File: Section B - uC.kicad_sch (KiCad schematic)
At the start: 8 parts, among them J1 Conn_ARM_SWD_TagConnect_TC203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, U1 ATtiny204-SS

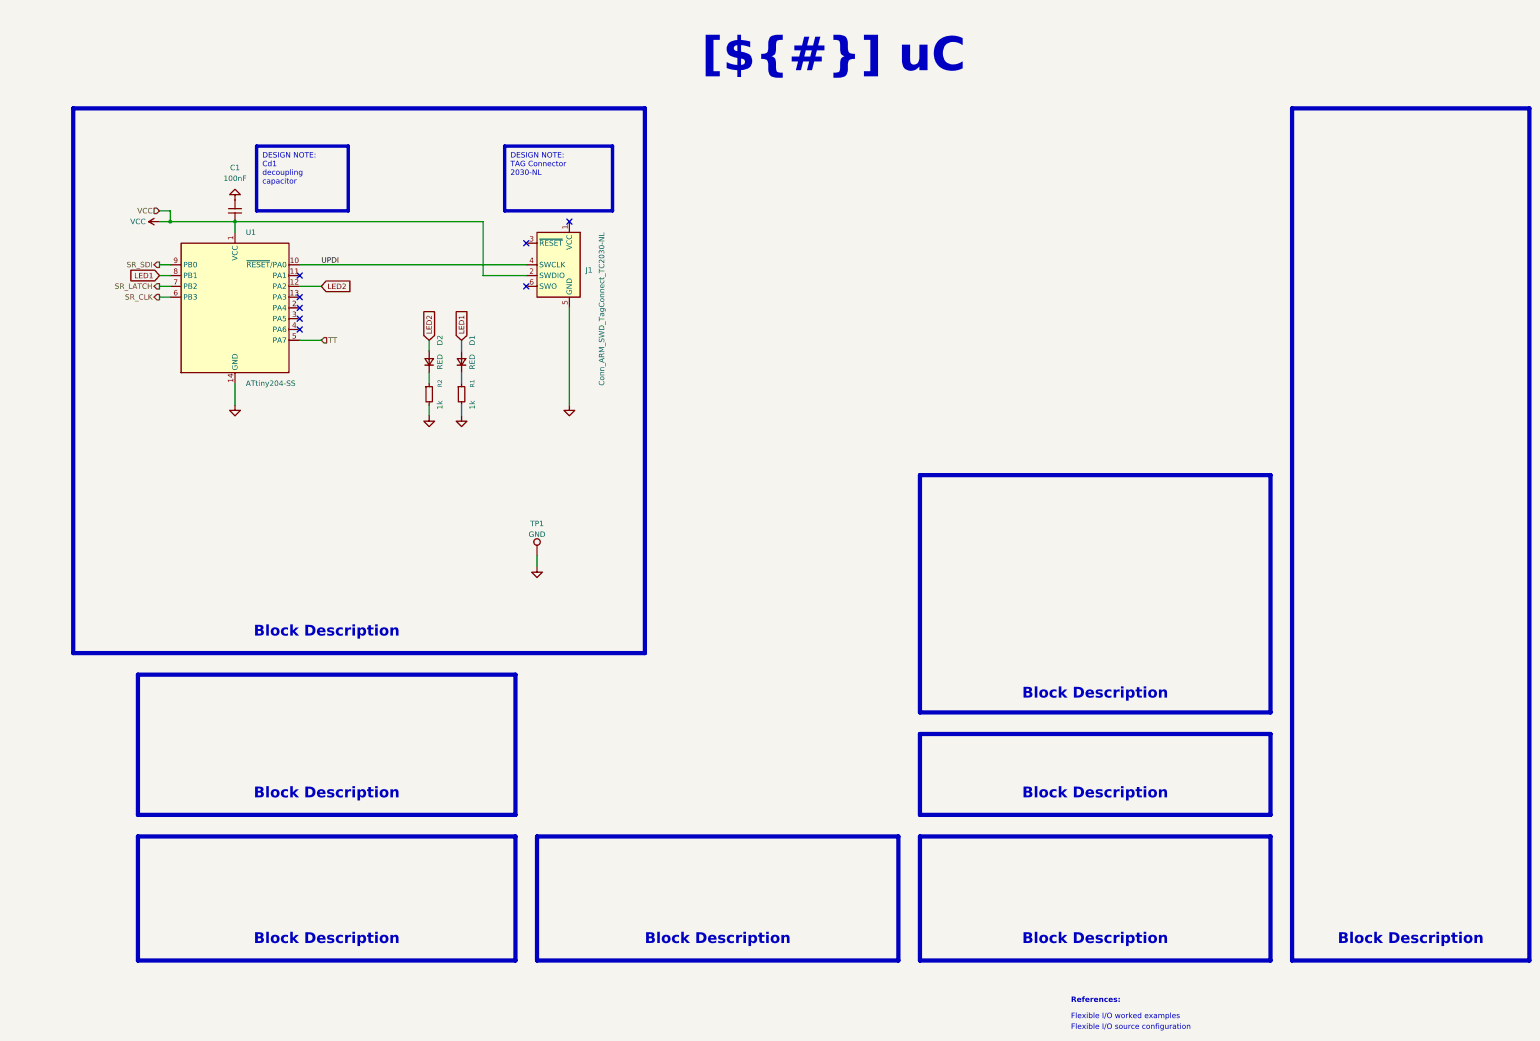
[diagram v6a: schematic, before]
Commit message: minor updates of shematic and pcb and touch pad library
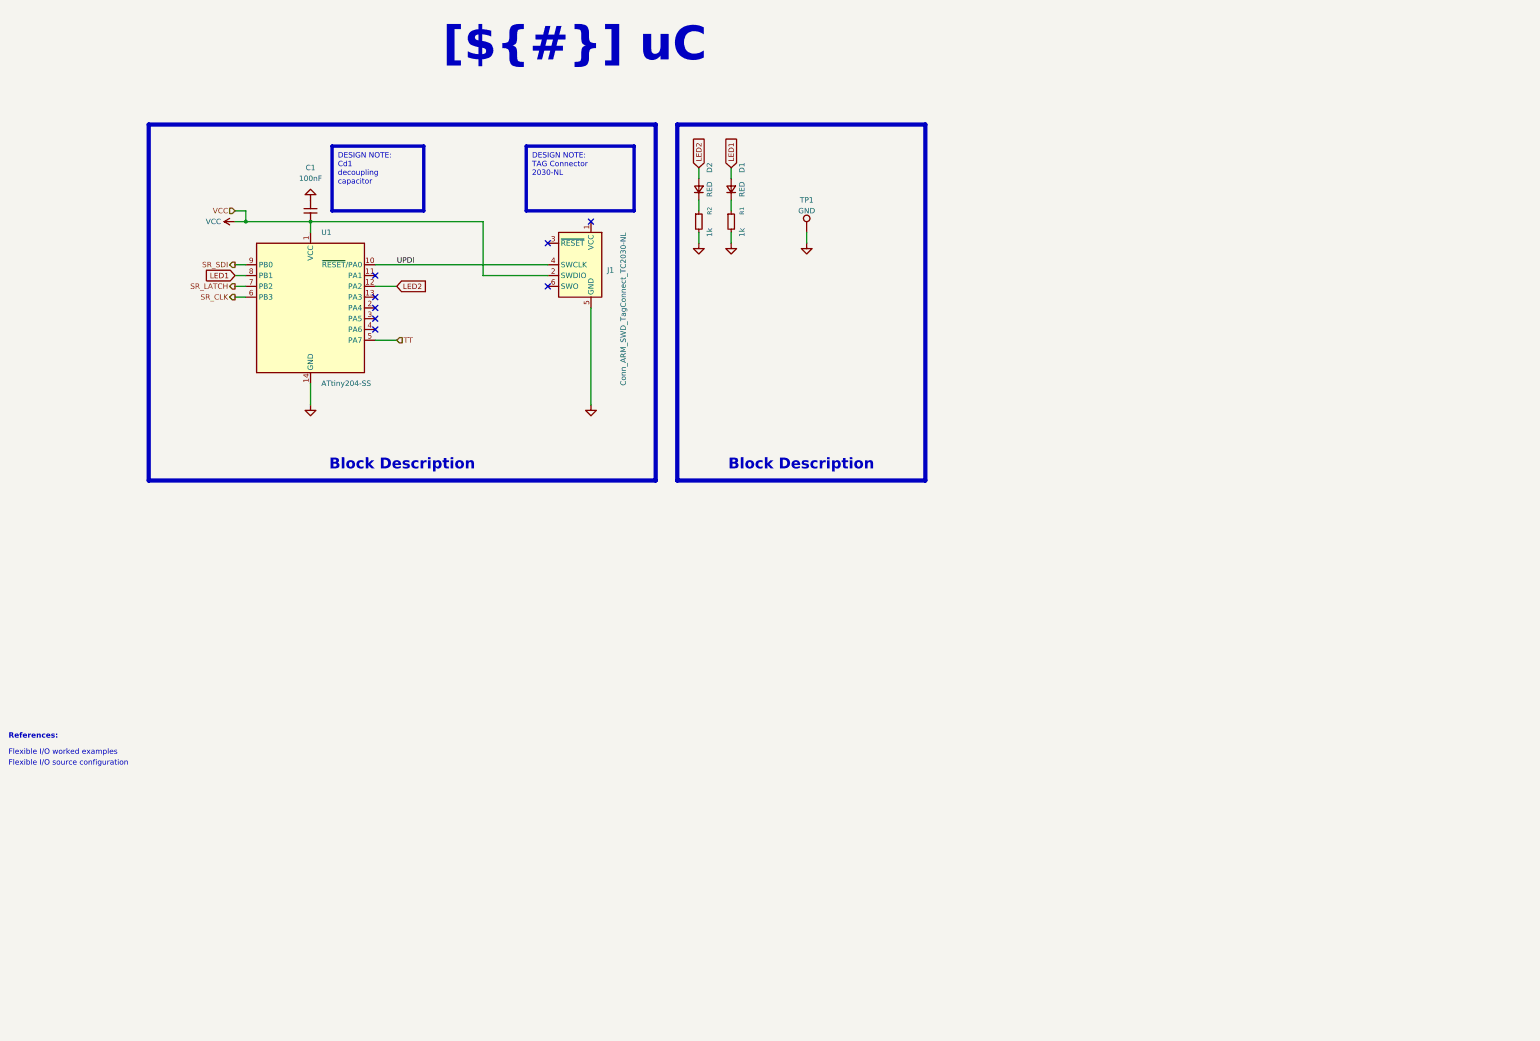
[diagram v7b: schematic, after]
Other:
- moved on the sheet: C1, D1, D2, J1, R1, R2, TP1, U1

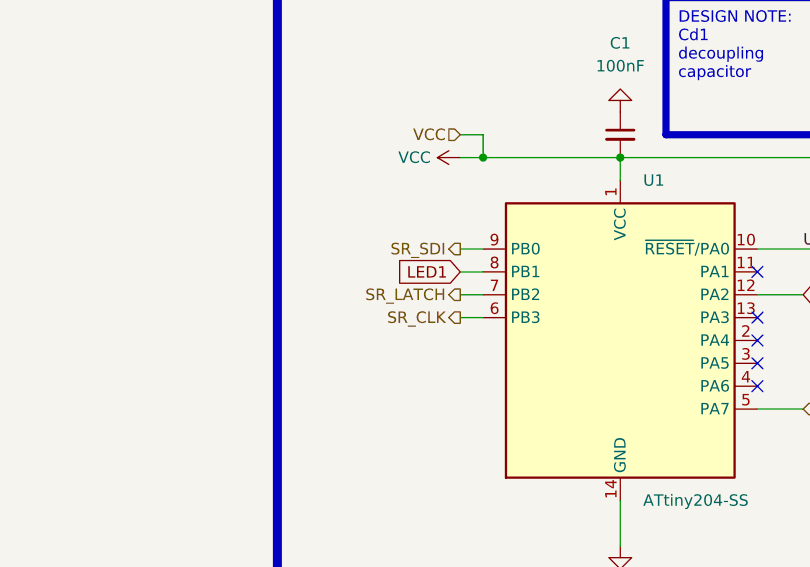
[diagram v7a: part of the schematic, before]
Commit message: [sch] update touch sensor section
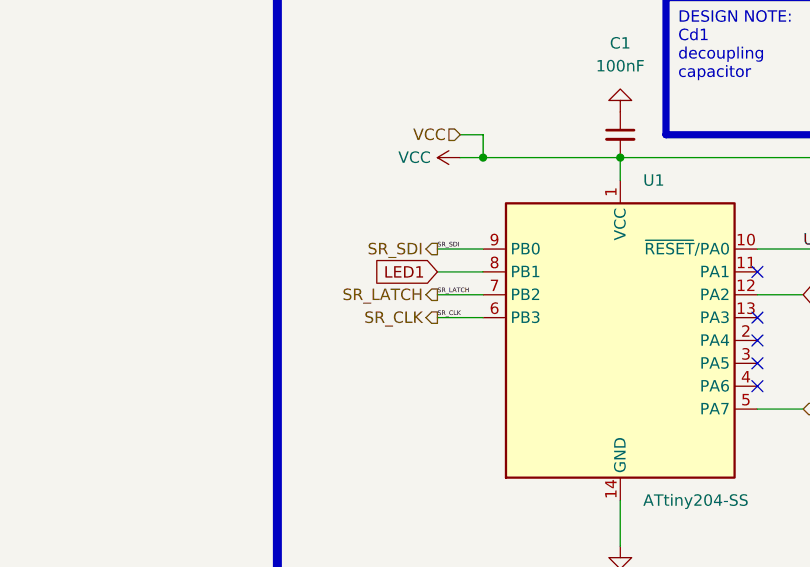
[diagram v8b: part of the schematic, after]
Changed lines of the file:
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@@
 	(wire
 		(pts
-			(xy 68.58 78.74) (xy 71.12 78.74)
+			(xy 66.04 78.74) (xy 71.12 78.74)
 		)
 		(stroke
@@
 	(wire
 		(pts
-			(xy 68.58 83.82) (xy 71.12 83.82)
+			(xy 66.04 83.82) (xy 71.12 83.82)
 		)
 		(stroke
@@
 	(wire
 		(pts
-			(xy 68.58 81.28) (xy 71.12 81.28)
+			(xy 66.04 81.28) (xy 71.12 81.28)
 		)
 		(stroke
@@
 	(wire
 		(pts
-			(xy 68.58 76.2) (xy 71.12 76.2)
-		)
-		(stroke
-			(width 0)
-			(type default)
+			(xy 66.04 76.2) (xy 71.12 76.2)
+		)
+		(stroke
+			(width 0)
+			(type default)
+		)
+	)
+	(label "SR_LATCH"
+		(at 66.04 81.28 0)
+		(effects
+			(font
+				(size 0.508 0.508)
+			)
+			(justify left bottom)
 		)
 	)
@@
 		)
 	)
+	(label "SR_SDI"
+		(at 66.04 76.2 0)
+		(effects
+			(font
+				(size 0.508 0.508)
+			)
+			(justify left bottom)
+		)
+	)
+	(label "SR_CLK"
+		(at 66.04 83.82 0)
+		(effects
+			(font
+				(size 0.508 0.508)
+			)
+			(justify left bottom)
+		)
+	)
 	(global_label "LED2"
 		(shape input)
@@
 	(global_label "LED1"
 		(shape input)
-		(at 68.58 78.74 180)
-		(fields_autoplaced yes)
-		(effects
-			(font
-				(size 1.27 1.27)
-			)
-			(justify right)
-		)
-		(property "Intersheetrefs" "${INTERSHEET_REFS}"
-			(at 60.9382 78.74 0)
+		(at 66.04 78.74 180)
+		(fields_autoplaced yes)
+		(effects
+			(font
+				(size 1.27 1.27)
+			)
+			(justify right)
+		)
+		(property "Intersheetrefs" "${INTERSHEET_REFS}"
+			(at 58.3982 78.74 0)
 			(effects
 				(font
@@
 	(hierarchical_label "SR_LATCH"
 		(shape output)
-		(at 68.58 81.28 180)
+		(at 66.04 81.28 180)
 		(effects
 			(font
@@
 	(hierarchical_label "SR_CLK"
 		(shape output)
-		(at 68.58 83.82 180)
+		(at 66.04 83.82 180)
 		(effects
 			(font
@@
 	(hierarchical_label "SR_SDI"
 		(shape output)
-		(at 68.58 76.2 180)
-		(effects
-			(font
+		(at 66.04 76.2 180)
+		(effects
+			(font
